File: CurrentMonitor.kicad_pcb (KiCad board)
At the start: 2 copper layers, 0 parts

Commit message: Initical placement of PCB components and edges. Still need USB parts.
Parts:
- added H1: MountingHole_Pad_3.5mm, MountingHole:MountingHole_3.5mm_Pad_Via, F.Cu at (50.8, 152.4)
- added H2: MountingHole_Pad_3.5mm, MountingHole:MountingHole_3.5mm_Pad_Via, F.Cu at (50.8, 73.6)
- added H3: MountingHole_Pad_3.5mm, MountingHole:MountingHole_3.5mm_Pad_Via, F.Cu at (152.4, 73.6)
- added H4: MountingHole_Pad_3.5mm, MountingHole:MountingHole_3.5mm_Pad_Via, F.Cu at (152.4, 152.4)
- added J10: Conn_01x05, Connector:Banana_Cliff_FCR7350x_S16N-PC_Horizontal, F.Cu at (146.0, 87.6)
- added J11: Conn_01x05, Connector:Banana_Cliff_FCR7350x_S16N-PC_Horizontal, F.Cu at (146.0, 106.7)
- added J13: Conn_Coaxial, Connector_Coaxial:BNC_Amphenol_B6252HB-NPP3G-50_Horizontal, F.Cu at (134.6, 147.3)
- added J2: Conn_01x05, Connector:Banana_Cliff_FCR7350x_S16N-PC_Horizontal, F.Cu at (57.2, 87.6)
- added J3: Conn_01x05, Connector:Banana_Cliff_FCR7350x_S16N-PC_Horizontal, F.Cu at (57.1, 106.7)
- added J5: Screw_Terminal_01x02, TerminalBlock_Phoenix:TerminalBlock_Phoenix_MKDS-1,5-2_1x02_P5.00mm_Horizontal, F.Cu at (50.8, 120.7)
- added J6: Screw_Terminal_01x02, TerminalBlock_Phoenix:TerminalBlock_Phoenix_MKDS-1,5-2_1x02_P5.00mm_Horizontal, F.Cu at (63.5, 152.4)
- added J7: Conn_02x03_Odd_Even, Connector_PinHeader_2.54mm:PinHeader_2x03_P2.54mm_Vertical, F.Cu at (108.0, 102.9)
- added J8: Screw_Terminal_01x02, TerminalBlock_Phoenix:TerminalBlock_Phoenix_MKDS-1,5-2_1x02_P5.00mm_Horizontal, F.Cu at (152.4, 125.7)
- added R1: 0.1R, Resistor_SMD:R_1206_3216Metric_Pad1.30x1.75mm_HandSolder, F.Cu at (84.1, 95.2)
- added R10: 0.1R, Resistor_SMD:R_1206_3216Metric_Pad1.30x1.75mm_HandSolder, F.Cu at (96.8, 114.3)
- added R2: 0.1R, Resistor_SMD:R_1206_3216Metric_Pad1.30x1.75mm_HandSolder, F.Cu at (84.1, 101.6)
- added R3: 0.1R, Resistor_SMD:R_1206_3216Metric_Pad1.30x1.75mm_HandSolder, F.Cu at (84.1, 108.0)
- added R4: 0.1R, Resistor_SMD:R_1206_3216Metric_Pad1.30x1.75mm_HandSolder, F.Cu at (84.1, 114.3)
- added R5: 10R, Resistor_SMD:R_1206_3216Metric_Pad1.30x1.75mm_HandSolder, F.Cu at (90.5, 76.2)
- added R6: 0.1R, Resistor_SMD:R_1206_3216Metric_Pad1.30x1.75mm_HandSolder, F.Cu at (96.8, 95.2)
- added R7: 1R, Resistor_SMD:R_1206_3216Metric_Pad1.30x1.75mm_HandSolder, F.Cu at (90.5, 82.5)
- added R8: 0.1R, Resistor_SMD:R_1206_3216Metric_Pad1.30x1.75mm_HandSolder, F.Cu at (96.8, 101.6)
- added R9: 0.1R, Resistor_SMD:R_1206_3216Metric_Pad1.30x1.75mm_HandSolder, F.Cu at (96.8, 108.0)
- added TP1: ID, TestPoint:TestPoint_Loop_D2.50mm_Drill1.0mm, F.Cu at (63.5, 133.3)
- added TP2: Rsense+, TestPoint:TestPoint_Loop_D2.50mm_Drill1.0mm, F.Cu at (76.2, 120.7)
- added TP3: TestPoint_2Pole, Connector:Banana_Jack_2Pin, F.Cu at (82.5, 146.1)
- added TP4: Rsense-, TestPoint:TestPoint_Loop_D2.50mm_Drill1.0mm, F.Cu at (108.0, 120.7)
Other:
- board outline added: 114.3 x 95.2 mm
- board text added: "10 Ohm 1 Ohm 0.1 Ohm"
- board text added: "Burden Resistor Selection"
- board text added: "Current Monitor ! Amused Scientist (Forrest) Lee Erickson Rev: 1.0 Date: 2024-03-04 SN:________________________________________"

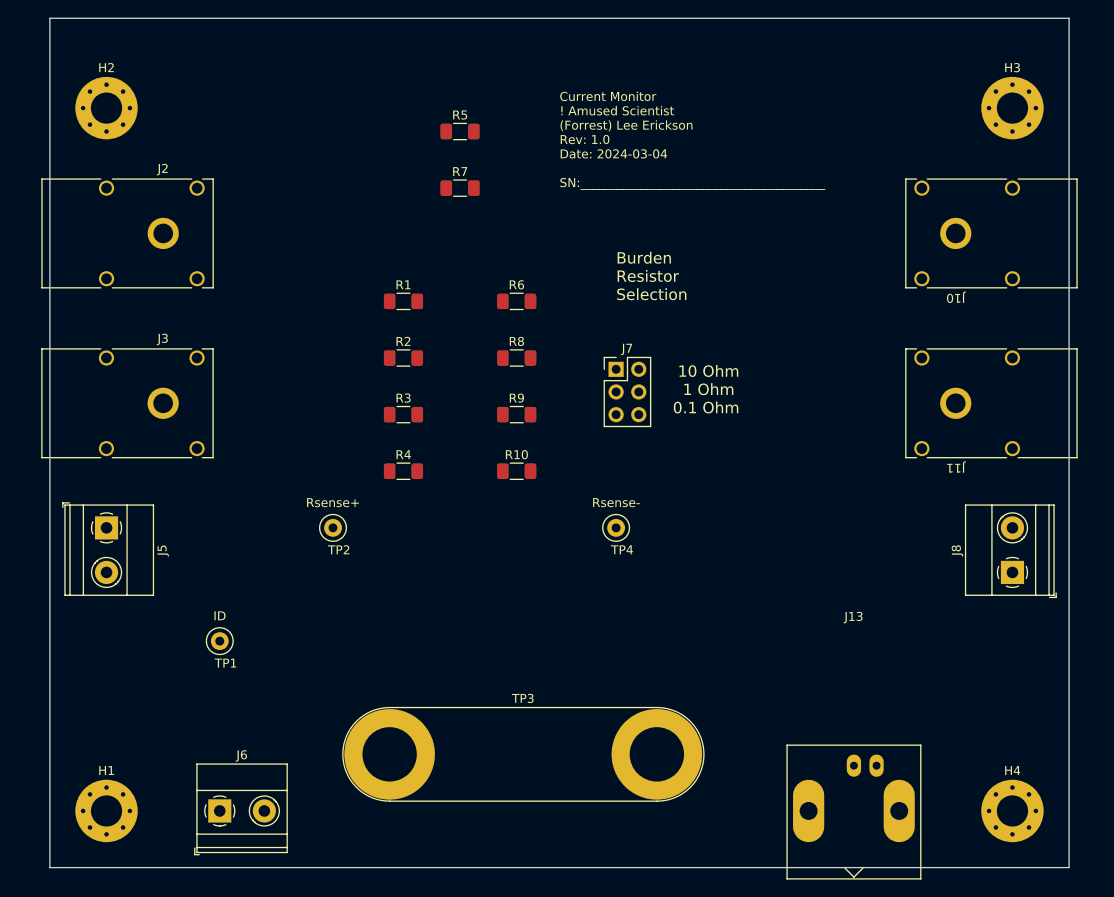
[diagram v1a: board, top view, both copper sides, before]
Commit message: Add another bananna jack option. Get 3D foot prints working for Barrel Jack.
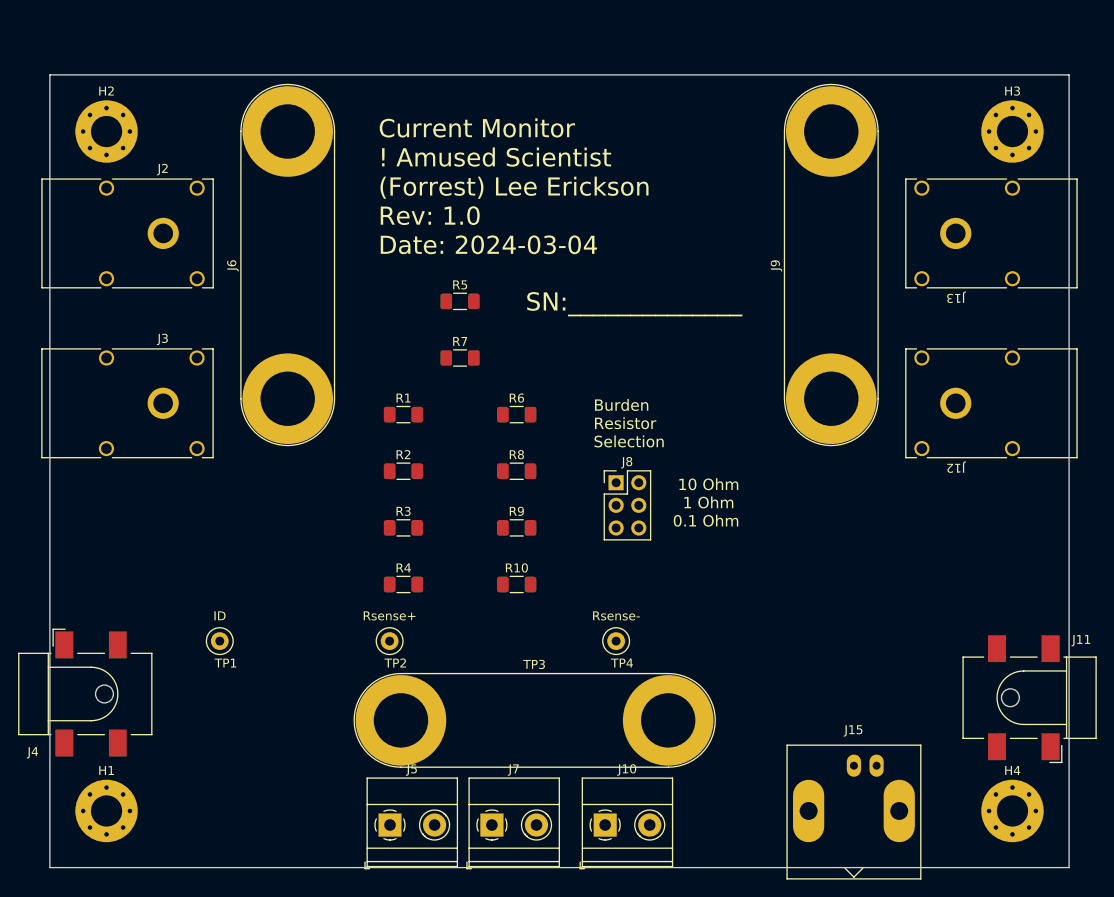
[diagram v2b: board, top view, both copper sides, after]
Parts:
- added J12: Conn_01x05, Connector:Banana_Cliff_FCR7350x_S16N-PC_Horizontal, F.Cu at (146.0, 106.7)
- added J15: Conn_Coaxial, Connector_Coaxial:BNC_Amphenol_B6252HB-NPP3G-50_Horizontal, F.Cu at (134.6, 147.3)
- added J4: Barrel_Jack_Switch_SMT, Connector_BarrelJack:BarrelJack_CLIFF_FC681465S_SMT_Horizontal, F.Cu at (49.1, 139.3)
- added J9: Conn_01x02_Socket, Connector:Banana_Jack_2Pin, F.Cu at (132.1, 106.2)
- J10: value Conn_01x05 -> Screw_Terminal_01x02; footprint Connector:Banana_Cliff_FCR7350x_S16N-PC_Horizontal -> TerminalBlock_Phoenix:TerminalBlock_Phoenix_MKDS-1,5-2_1x02_P5.00mm_Horizontal
- J11: value Conn_01x05 -> Barrel_Jack_Switch_SMT; footprint Connector:Banana_Cliff_FCR7350x_S16N-PC_Horizontal -> Connector_BarrelJack:BarrelJack_CLIFF_FC681465S_SMT_Horizontal
- J13: value Conn_Coaxial -> Conn_01x05; footprint Connector_Coaxial:BNC_Amphenol_B6252HB-NPP3G-50_Horizontal -> Connector:Banana_Cliff_FCR7350x_S16N-PC_Horizontal
- J6: value Screw_Terminal_01x02 -> Conn_01x02_Socket; footprint TerminalBlock_Phoenix:TerminalBlock_Phoenix_MKDS-1,5-2_1x02_P5.00mm_Horizontal -> Connector:Banana_Jack_2Pin
- J7: value Conn_02x03_Odd_Even -> Screw_Terminal_01x02; footprint Connector_PinHeader_2.54mm:PinHeader_2x03_P2.54mm_Vertical -> TerminalBlock_Phoenix:TerminalBlock_Phoenix_MKDS-1,5-2_1x02_P5.00mm_Horizontal
- J8: value Screw_Terminal_01x02 -> Conn_02x03_Odd_Even; footprint TerminalBlock_Phoenix:TerminalBlock_Phoenix_MKDS-1,5-2_1x02_P5.00mm_Horizontal -> Connector_PinHeader_2.54mm:PinHeader_2x03_P2.54mm_Vertical
- moved J10 77.1 mm to (106.7, 154.0), turned to 0 degrees
- moved J13 60.8 mm to (146.0, 87.6)
- moved J7 53.0 mm to (94.0, 154.0)
- moved J6 46.9 mm to (71.1, 106.2), turned to 90 degrees
- moved J5 46.1 mm to (82.6, 154.0), turned to 0 degrees
- moved J8 45.6 mm to (108.0, 115.6), turned to 0 degrees
- moved J11 33.9 mm to (153.7, 139.7)
- moved R5 19.0 mm to (90.5, 95.2)
- moved R7 19.0 mm to (90.5, 101.6)
- moved TP2 14.2 mm to (82.5, 133.3)
- moved R1 12.7 mm to (84.1, 108.0)
- moved R10 12.7 mm to (96.8, 127.0)
- moved R2 12.7 mm to (84.1, 114.3)
- moved R3 12.7 mm to (84.1, 120.7)
- moved R4 12.7 mm to (84.1, 127.0)
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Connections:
- J10 pad 1: unconnected-(J10-Pin_1-Pad1) -> GND
- J11 pad 1: unconnected-(J11-Pin_1-Pad1) -> Net-(J10-Pin_2)
- J13 pad 1: Net-(J10-Pin_5) -> unconnected-(J13-Pin_1-Pad1)
- J6 pad 1: Net-(J1-VBUS) -> GND
- J6 pad 2: Net-(J10-Pin_5) -> Net-(J1-VBUS)
- J7 pad 1: Net-(J7-Pin_1) -> Net-(J1-VBUS)
- J7 pad 2: Net-(J10-Pin_5) -> Net-(J10-Pin_2)
- J8 pad 1: GND -> Net-(J8-Pin_1)
- J8 pad 2: Net-(J10-Pin_5) -> Net-(J10-Pin_2)
- R10 pad 2: Net-(J7-Pin_5) -> Net-(J8-Pin_5)
- R5 pad 2: Net-(J7-Pin_1) -> Net-(J8-Pin_1)
- R6 pad 2: Net-(J7-Pin_5) -> Net-(J8-Pin_5)
- R7 pad 2: Net-(J7-Pin_3) -> Net-(J8-Pin_3)
- R8 pad 2: Net-(J7-Pin_5) -> Net-(J8-Pin_5)
- R9 pad 2: Net-(J7-Pin_5) -> Net-(J8-Pin_5)
- TP3 pad 2: Net-(J10-Pin_5) -> Net-(J10-Pin_2)
- TP4 pad 1: Net-(J10-Pin_5) -> Net-(J10-Pin_2)
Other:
- board size 114.3 x 95.2 mm -> 114.3 x 88.9 mm
- board text added: "Current Monitor ! Amused Scientist (Forrest) Lee Erickson Rev: 1.0 Date: 2024-03-04"
- board text added: "SN:______________"
- board text removed: "Current Monitor ! Amused Scientist (Forrest) Lee Erickson Rev: 1.0 Date: 2024-03-04 SN:________________________________________"

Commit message: Update with USB type A footprint. Update footprint of Barrel jack, mounting holes and bannana jacks. No ERC errors.
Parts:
- added J1: USB_B_Micro_Local, PubInv_KiCad_PCB:USB_Micro-B_Amphenol_10118194_Horizontal, F.Cu at (47.2, 139.7)
- added J14: USB_A, PubInv_KiCad_PCB:USB_A_JLCPCB_C3038692_Horizontal, F.Cu at (149.8, 140.0)
- H1, H2, H3, H4: value MountingHole_Pad_3.5mm -> MountingHole_Pad
- J11, J4: footprint Connector_BarrelJack:BarrelJack_CLIFF_FC681465S_SMT_Horizontal -> PubInv_KiCad_PCB:BarrelJack_CLIFF_FC681465S_SMT_Horizontal
- J12, J13, J2, J3: footprint Connector:Banana_Cliff_FCR7350x_S16N-PC_Horizontal -> PubInv_KiCad_PCB:Banana_Cliff_FCR7350x_S16N-PC_Horizontal_5Pins
- moved J12 19.1 mm to (146.0, 87.6)
- moved J13 19.1 mm to (146.0, 106.7)
- moved J11 17.1 mm to (153.7, 122.6)
- moved J4 16.7 mm to (49.0, 122.6)
- moved J5 14.6 mm to (68.0, 154.0)
- moved TP4 7.75 mm to (103.5, 127.0)
- moved TP2 7.75 mm to (78.1, 127.0)
- moved TP3 5.08 mm to (83.8, 137.2)
- moved J10 4.45 mm to (111.2, 154.0)
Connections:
- J12 pad 1: unconnected-(J12-Pin_1-Pad1) -> Net-(J10-Pin_2)
- J13 pad 1: unconnected-(J13-Pin_1-Pad1) -> GND
- J2 pad 1: unconnected-(J2-Pin_1-Pad1) -> Net-(J1-VBUS)
- J3 pad 1: unconnected-(J3-Pin_1-Pad1) -> GND
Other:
- board text added: "V_Rsense"
- board text added: "Vin"
- board text added: "Vout"

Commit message: Route copper on PCB.
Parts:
- J7: value Screw_Terminal_01x02 -> Screw_Terminal_01x03; footprint TerminalBlock_Phoenix:TerminalBlock_Phoenix_MKDS-1,5-2_1x02_P5.00mm_Horizontal -> TerminalBlock_Phoenix:TerminalBlock_Phoenix_MKDS-1,5-3_1x03_P5.00mm_Horizontal
- moved TP1 14.5 mm to (56.5, 146.1)
- moved J7 3.30 mm to (91.6, 151.8)
- moved J11 1.91 mm to (111.1, 152.1)
- moved J5 1.91 mm to (68.0, 152.1)
- renumbered J9 to J10, J10 to J11, J11 to J12, J12 to J13, J13 to J14, J14 to J15, J15 to J16, J8 to J9
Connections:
- net Net-(J1-D+) renamed /D+
- net Net-(J1-D-) renamed /D-
- net Net-(J1-VBUS) renamed /+Vin
- net Net-(J8-Pin_1) renamed /+Vburd10R
- net Net-(J8-Pin_3) renamed /+Vburd1R0
- net Net-(J8-Pin_5) renamed /+Vburd0R1
- J10 pad 2: Net-(J10-Pin_2) -> /+Vout
- J11 pad 2: Net-(J10-Pin_2) -> /+Vout
- J12 pad 1: Net-(J10-Pin_2) -> /+Vout
- J12 pad 4: Net-(J10-Pin_2) -> /+Vout
- J13 pad 1: Net-(J10-Pin_2) -> /+Vout
- J15 pad 1: Net-(J10-Pin_2) -> /+Vout
- J16 pad 1: Net-(J10-Pin_2) -> /+Vout
- J7 pad 2: Net-(J10-Pin_2) -> GND
- J9 pad 2: Net-(J10-Pin_2) -> /+Vout
- J9 pad 4: Net-(J10-Pin_2) -> /+Vout
- J9 pad 6: Net-(J10-Pin_2) -> /+Vout
- TP3 pad 2: Net-(J10-Pin_2) -> /+Vout
- TP4 pad 1: Net-(J10-Pin_2) -> /+Vout
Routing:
- net /+Vin: track 0.00 -> 228.0 mm, vias 0 -> 2
- net /+Vout: track 0.00 -> 210.3 mm, vias 0 -> 1
- net /D-: track 0.00 -> 111.2 mm, vias 0 -> 2
- net /D+: track 0.00 -> 108.5 mm, vias 0 -> 2
- net /+Vburd1R0: track 0.00 -> 29.1 mm
- net /+Vburd0R1: track 0.00 -> 28.7 mm
- net /+Vburd10R: track 0.00 -> 28.1 mm
- net Net-(J1-ID): track 0.00 -> 10.2 mm
- net Net-(R3-Pad2): track 0.00 -> 9.60 mm
- net Net-(R2-Pad2): track 0.00 -> 9.60 mm
- net Net-(R10-Pad1): track 0.00 -> 9.60 mm
- net Net-(R1-Pad2): track 0.00 -> 9.60 mm
- net GND: track 0.00 -> 2.82 mm, vias 0 -> 18
- added copper zone on B.Cu, net GND
- added copper zone on F.Cu, net GND
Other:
- board text added: "GND"
- board text added: "USB Vin"
